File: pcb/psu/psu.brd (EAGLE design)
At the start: 86.4 x 54.7 mm, 32 parts, among them J1 BATTERY_CONNDEANS, U1 EEPROM-I2CSMD, U2 LM2596, U3 LM2596

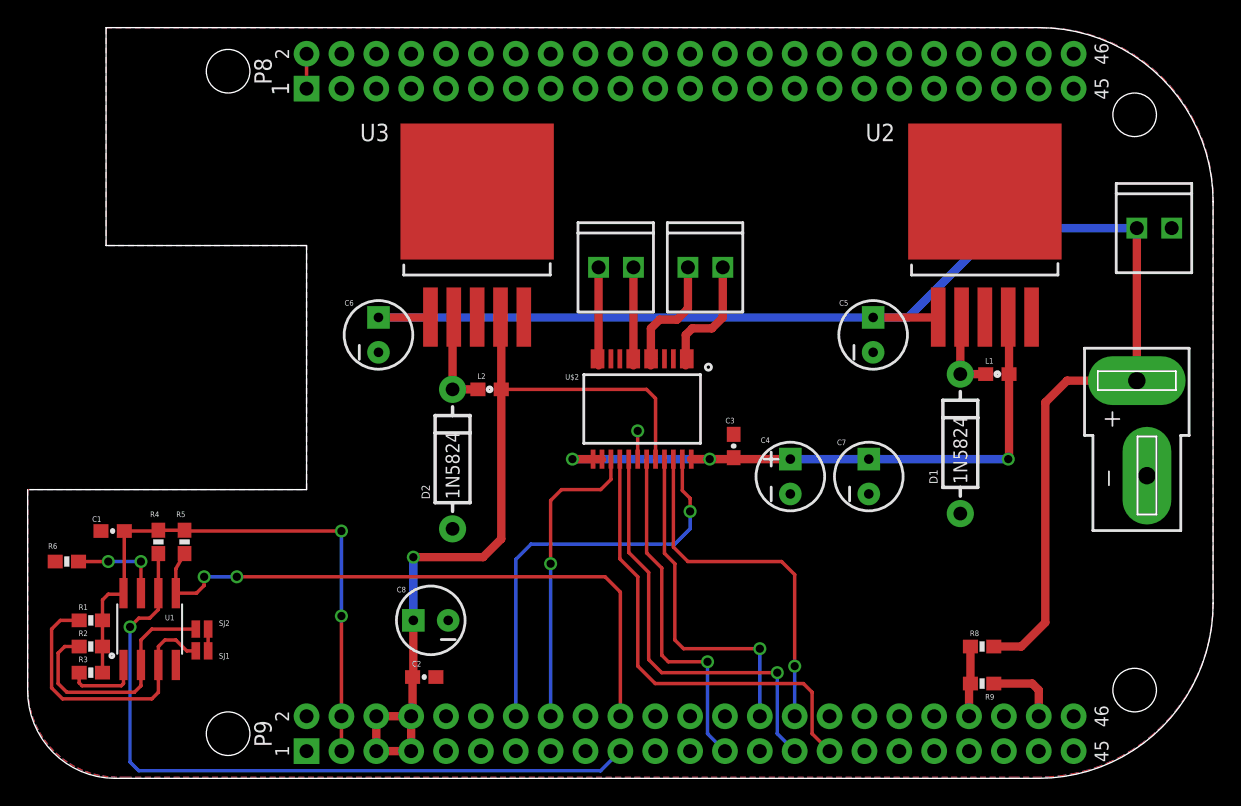
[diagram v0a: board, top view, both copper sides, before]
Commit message: Updated board layout and changed deans connector to screw terminal
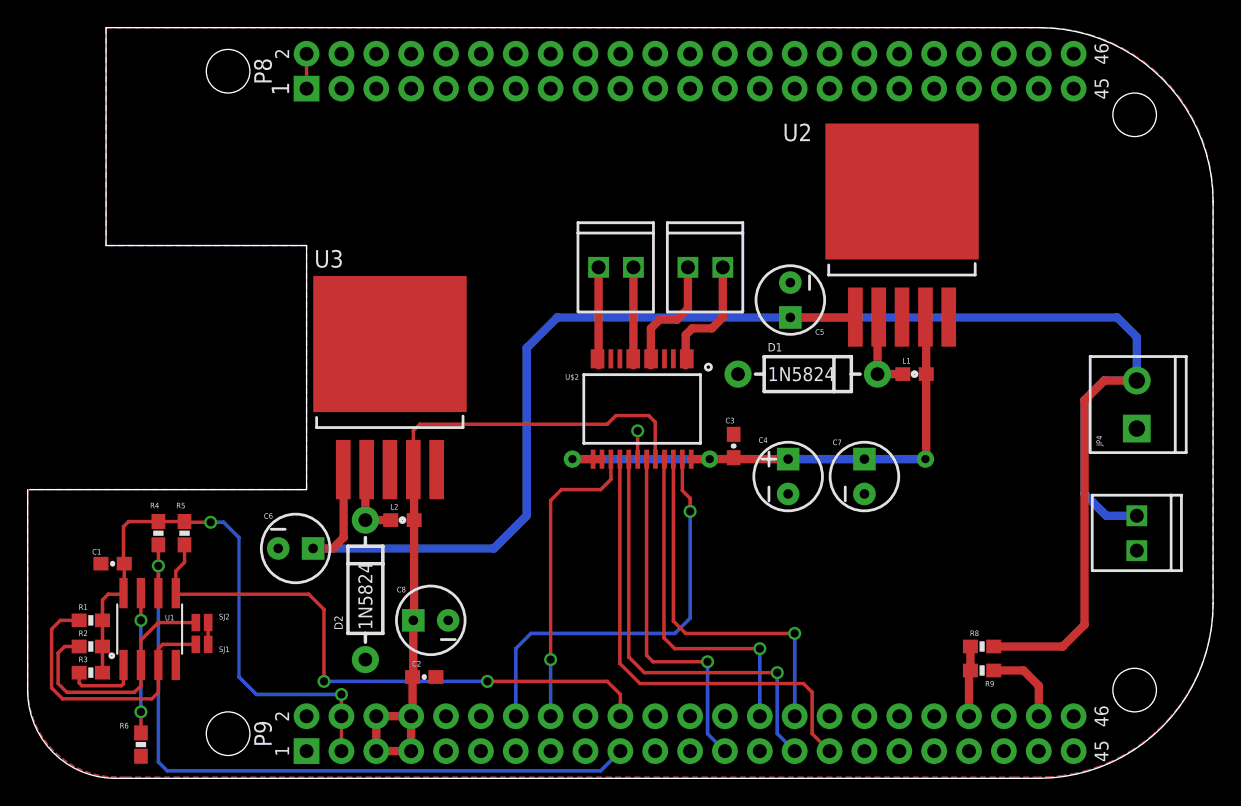
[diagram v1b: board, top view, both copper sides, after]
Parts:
- removed J1: BATTERY_CONNDEANS, SparkFun-Connectors:DEANS
- added JP4: (no value), SparkFun-Connectors:SCREWTERMINAL-3.5MM-2
- L1, L2: value 33 uH -> 68 uH
- moved JP1 21.0 mm to (80.8, 19.1), turned to 270 degrees
- moved C6 16.7 mm to (19.5, 16.7), turned to 0 degrees
- moved R6 14.4 mm to (8.26, 2.38), turned to 90 degrees
- moved U3 12.8 mm to (20.8, 36.5)
- moved D1 12.2 mm to (56.8, 29.4), turned to 0 degrees
- moved D2 11.4 mm to (24.6, 13.7)
- moved L2 11.4 mm to (27.3, 18.7)
- moved C5 6.55 mm to (55.6, 34.8), turned to 270 degrees
- moved U2 6.03 mm to (58.1, 47.6)
- moved L1 6.03 mm to (64.6, 29.4)
- moved C1 2.38 mm to (6.19, 15.6)
- moved R9 0.95 mm to (69.5, 7.78)
- moved R4 0.64 mm to (9.53, 17.8)
- moved R5 0.64 mm to (11.4, 17.8)
- moved SJ1 0.48 mm to (12.7, 9.68)
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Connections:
- net GND: now also JP4.1; no longer J1.-
- net V_BATT: now also JP4.2; no longer J1.+
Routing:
- net V_BATT: track 105.4 -> 133.9 mm
- net V_CPU: track 60.9 -> 52.0 mm, vias 1 -> 0
- net V_MOTOR: track 45.9 -> 39.7 mm
- net N$5: track 6.85 -> 10.2 mm
- net SDA: track 45.8 -> 43.9 mm
- net N$9: track 7.12 -> 5.57 mm
- net GND: track 12.0 -> 13.0 mm
- net SCL: track 53.1 -> 52.3 mm
- net BIN1: track 31.2 -> 31.9 mm
- net STBY: track 25.3 -> 26.0 mm
- net BIN2: track 33.9 -> 34.6 mm
- net AIN2: track 26.4 -> 27.0 mm
- net N$3: track 21.4 -> 20.9 mm

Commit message: Lots of routing tweaks
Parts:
- added R10, R7: 0, SparkFun-Resistors:0603-RES
- moved C5 2.86 mm to (55.7, 31.9)
- moved U2 2.86 mm to (58.1, 44.8)
- moved D1 2.70 mm to (56.8, 26.7)
- moved L1 2.70 mm to (64.6, 26.7)
- moved C3 1.75 mm to (51.6, 22.4), turned to 270 degrees
- moved C8 0.95 mm to (29.4, 10.5)
- moved C2 0.63 mm to (28.9, 6.67)
- moved JP1 0.32 mm to (81.1, 19.1)
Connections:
- new net SCL_PRE: R4.1, R7.1, U1.6
- new net SDA_PRE: R10.1, R5.1, U1.5
- net SCL: now also R7.2; no longer R4.1, U1.6
- net SDA: now also R10.2; no longer R5.1, U1.5
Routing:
- net SCL: track 52.3 -> 32.6 mm, vias 1 -> 2
- net SCL_PRE: track 0.00 -> 15.2 mm, vias 0 -> 2
- net SDA: track 43.9 -> 29.7 mm
- net SDA_PRE: track 0.00 -> 11.4 mm
- net V_BATT: track 133.9 -> 130.8 mm
- net V_MOTOR: track 39.7 -> 40.8 mm, vias 3 -> 2
- net 3.3V: track 43.3 -> 43.2 mm, vias 2 -> 1

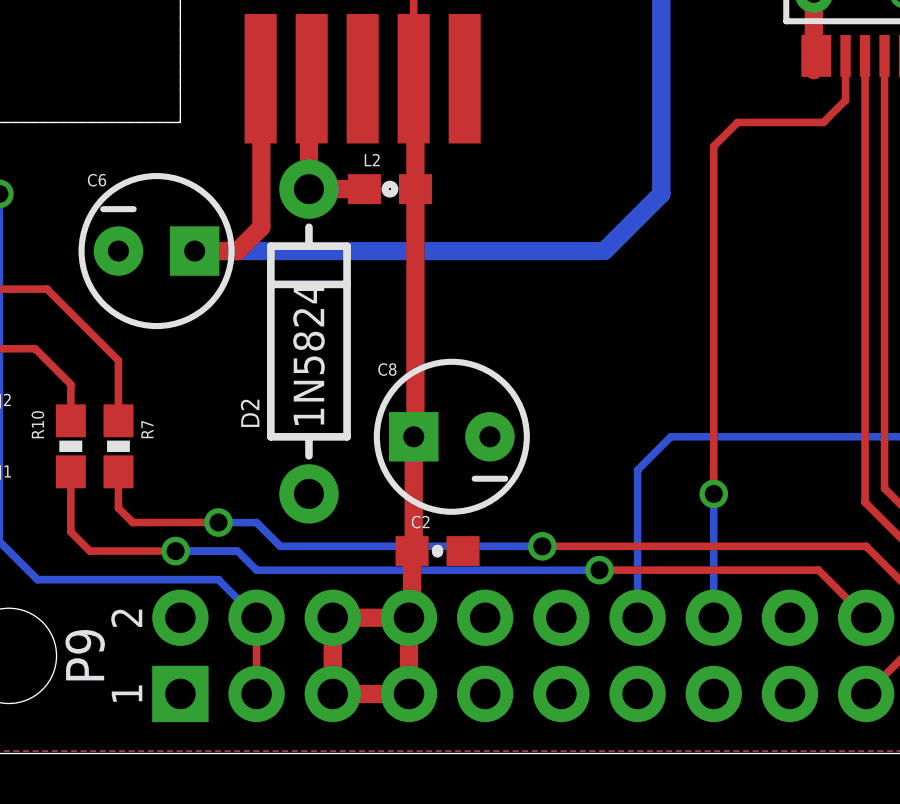
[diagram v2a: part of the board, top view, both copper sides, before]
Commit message: Filled pours
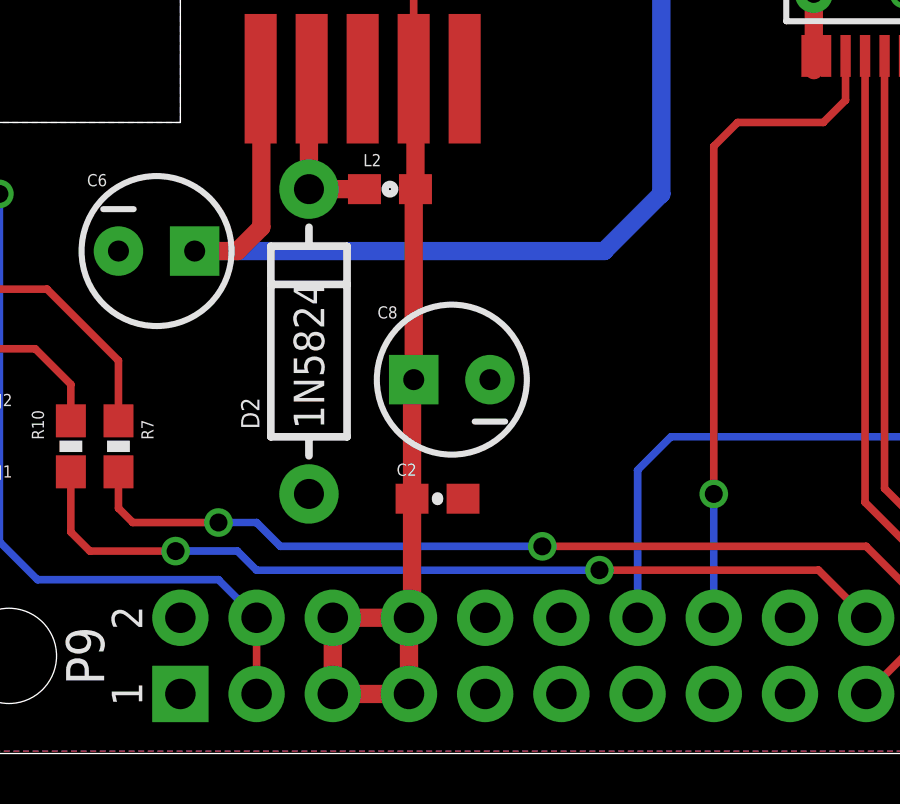
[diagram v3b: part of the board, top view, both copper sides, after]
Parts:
- moved C8 1.91 mm to (29.4, 12.4)
- moved C2 1.75 mm to (28.9, 8.41)
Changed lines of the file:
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@@
 <element name="JP2" library="SparkFun-Connectors" package="1X02_2.54_SCREWTERM" value="" x="48.10125" y="37.1475"/>
 <element name="JP3" library="SparkFun-Connectors" package="1X02_2.54_SCREWTERM" value="" x="41.5925" y="37.1475"/>
-<element name="C2" library="SparkFun-Capacitors" package="0603-CAP" value="0.1uF" x="28.8925" y="6.6675">
-<attribute name="PROD_ID" value="CAP-00810" x="28.8925" y="6.6675" size="1.778" layer="27" display="off"/>
+<element name="C2" library="SparkFun-Capacitors" package="0603-CAP" value="0.1uF" x="28.8925" y="8.41375" smashed="yes">
+<attribute name="PROD_ID" value="CAP-00810" x="28.8925" y="8.41375" size="1.778" layer="27" display="off"/>
+<attribute name="NAME" x="27.52725" y="9.17575" size="0.4064" layer="25" font="vector"/>
+<attribute name="VALUE" x="27.8765" y="7.27075" size="0.4064" layer="27" font="vector"/>
 </element>
 <element name="C3" library="SparkFun-Capacitors" package="0603-CAP" value="0.1uF" x="51.59375" y="22.38375" smashed="yes" rot="R270">
@@
 <element name="L1" library="SparkFun-Passives" package="0603" value="68 uH" x="64.61125" y="26.67"/>
 <element name="D1" library="SparkFun-DiscreteSemi" package="DIODE-1N4001" value="1N5824" x="56.8325" y="26.67"/>
-<element name="C8" library="SparkFun-Capacitors" package="CPOL-RADIAL-10UF-25V" value="220 uF" x="29.36875" y="10.4775" smashed="yes" rot="R180">
-<attribute name="NAME" x="27.559" y="12.92225" size="0.4064" layer="25" rot="R180"/>
+<element name="C8" library="SparkFun-Capacitors" package="CPOL-RADIAL-10UF-25V" value="220 uF" x="29.36875" y="12.3825" smashed="yes" rot="R180">
+<attribute name="NAME" x="27.559" y="14.82725" size="0.4064" layer="25" rot="R180"/>
 </element>
 <element name="L2" library="SparkFun-Passives" package="0603" value="68 uH" x="27.305" y="18.7325" smashed="yes">
@@
 <contactref element="U3" pad="4"/>
 <contactref element="L2" pad="2"/>
-<wire x1="28.09875" y1="10.4775" x2="28.09875" y2="6.72375" width="0.6096" layer="1"/>
-<wire x1="28.09875" y1="6.72375" x2="28.0425" y2="6.6675" width="0.6096" layer="1"/>
-<wire x1="28.0425" y1="6.6675" x2="28.0425" y2="4.5475" width="0.6096" layer="1"/>
-<wire x1="28.0425" y1="4.5475" x2="27.94" y2="4.445" width="0.6096" layer="1"/>
-<wire x1="28.155" y1="18.7325" x2="28.155" y2="10.58" width="0.6096" layer="1"/>
-<wire x1="28.155" y1="10.58" x2="28.09875" y2="10.4775" width="0.6096" layer="1"/>
 <wire x1="28.155" y1="18.7325" x2="28.155" y2="21.995" width="0.6096" layer="1"/>
 <wire x1="28.155" y1="21.995" x2="28.09625" y2="22.4125" width="0.6096" layer="1"/>
@@
 <wire x1="45.72" y1="25.87625" x2="45.72" y2="23.19525" width="0.254" layer="1"/>
 <wire x1="45.72" y1="23.19525" x2="45.7425" y2="23.17275" width="0.254" layer="1"/>
+<wire x1="28.0425" y1="8.41375" x2="28.0425" y2="4.5475" width="0.6096" layer="1"/>
+<wire x1="28.0425" y1="4.5475" x2="27.94" y2="4.445" width="0.6096" layer="1"/>
+<wire x1="28.0425" y1="8.41375" x2="28.0425" y2="12.32625" width="0.6096" layer="1"/>
+<wire x1="28.0425" y1="12.32625" x2="28.09875" y2="12.3825" width="0.6096" layer="1"/>
+<wire x1="28.09875" y1="12.3825" x2="28.09875" y2="18.67625" width="0.6096" layer="1"/>
+<wire x1="28.09875" y1="18.67625" x2="28.155" y2="18.7325" width="0.6096" layer="1"/>
 </signal>
 <signal name="V_MOTOR">
